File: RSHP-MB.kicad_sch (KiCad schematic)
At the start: 23 parts, among them J1 Conn_02x20_Odd_Even, J2 Conn_02x02_Odd_Even, J3 Conn_02x02_Odd_Even, J4 Conn_02x04_Odd_Even

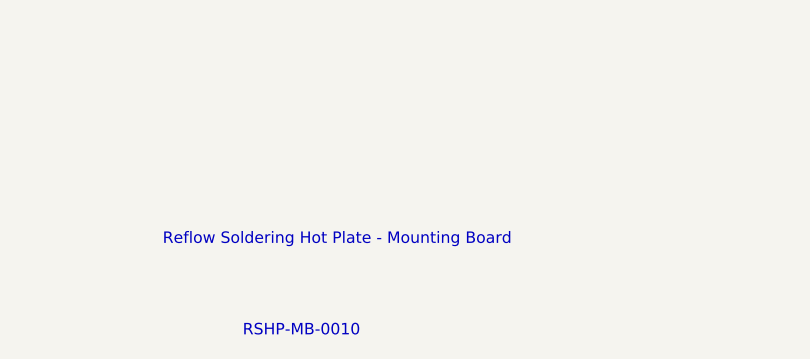
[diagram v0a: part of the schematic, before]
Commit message: Properly filled document metadata
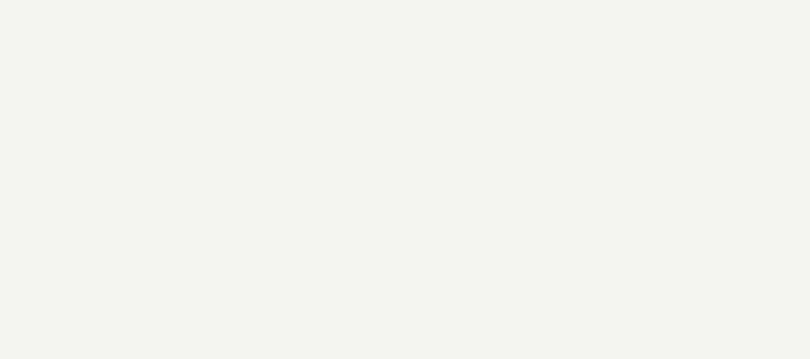
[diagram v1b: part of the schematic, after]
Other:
- note removed: "RSHP-MB-0010"
- note removed: "Reflow Soldering Hot Plate - Mounting Board"
- company: (none) -> (c) Andriy Golovnya http://redscorp.net
- title: (none) -> RSHP-MB-0010
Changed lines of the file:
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@@
 (kicad_sch (version 20211123) (generator eeschema)
   (paper "A4")
+  (title_block
+    (title "RSHP-MB-0010")
+    (date "2022-05-21")
+    (rev "1.0")
+    (company "(c) Andriy Golovnya http://redscorp.net")
+    (comment 1 "Reflow Soldering Hot Plate - Mounting Board")
+  )
   (junction (at 76.2 83.82) (diameter 0) (color 0 0 0 0)
   )
@@
   (wire (pts (xy 39.37 121.92) (xy 39.37 127))
     (stroke (width 0) (type default) (color 0 0 0 0))
-  )
-  (text "RSHP-MB-0010" (at 186.69 190.5 0)
-    (effects (font (size 1.27 1.27)) (justify left bottom))
   )
   (text "Fan Mounting Holes/\nEarth Tranfer Points" (at 134.62 114.3 0)
@@
     (effects (font (size 1.27 1.27) bold) (justify left bottom))
   )
-  (text "Reflow Soldering Hot Plate - Mounting Board" (at 177.8 180.34 0)
-    (effects (font (size 1.27 1.27)) (justify left bottom))
-  )
   (text "Thermal Resistors Connector" (at 198.12 38.1 0)

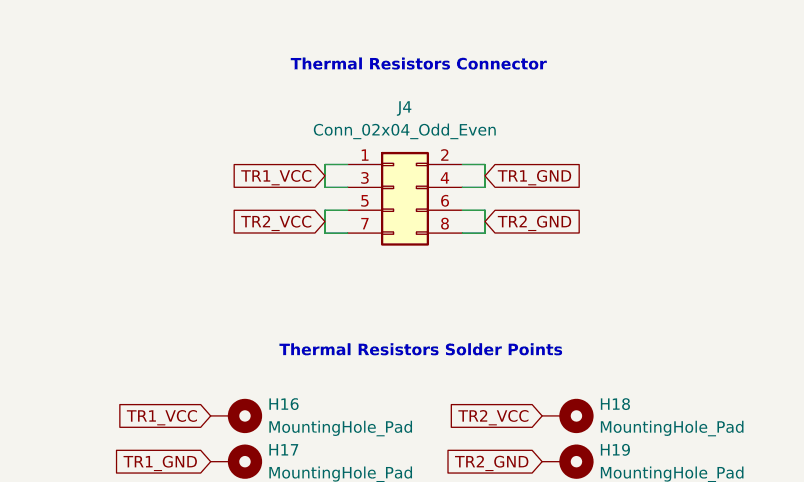
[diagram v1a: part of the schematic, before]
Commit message: Switched TR connector sides in schematics. rounded some corners on PCB.
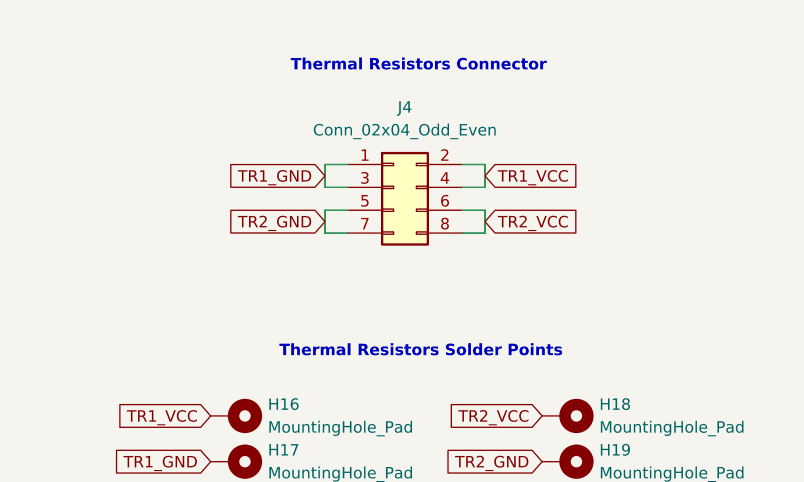
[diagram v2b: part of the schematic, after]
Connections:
- net TR1_GND: now also J4.1 (Pin_1), J4.3 (Pin_3); no longer J4.2 (Pin_2), J4.4 (Pin_4)
- net TR1_VCC: now also J4.2 (Pin_2), J4.4 (Pin_4); no longer J4.1 (Pin_1), J4.3 (Pin_3)
- net TR2_GND: now also J4.5 (Pin_5), J4.7 (Pin_7); no longer J4.6 (Pin_6), J4.8 (Pin_8)
- net TR2_VCC: now also J4.6 (Pin_6), J4.8 (Pin_8); no longer J4.5 (Pin_5), J4.7 (Pin_7)
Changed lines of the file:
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@@
     )
   )
-  (global_label "TR2_VCC" (shape input) (at 201.93 54.61 180) (fields_autoplaced)
-    (effects (font (size 1.27 1.27)) (justify right))
-    (property "Intersheet References" "${INTERSHEET_REFS}" (id 0) (at 191.4736 54.6894 0)
-      (effects (font (size 1.27 1.27)) (justify right) hide)
+  (global_label "TR2_VCC" (shape input) (at 219.71 54.61 0) (fields_autoplaced)
+    (effects (font (size 1.27 1.27)) (justify left))
+    (property "Intersheet References" "${INTERSHEET_REFS}" (id 0) (at 230.1664 54.5306 0)
+      (effects (font (size 1.27 1.27)) (justify left) hide)
     )
   )
-  (global_label "TR2_GND" (shape input) (at 219.71 54.61 0) (fields_autoplaced)
-    (effects (font (size 1.27 1.27)) (justify left))
-    (property "Intersheet References" "${INTERSHEET_REFS}" (id 0) (at 230.4083 54.6894 0)
-      (effects (font (size 1.27 1.27)) (justify left) hide)
+  (global_label "TR2_GND" (shape input) (at 201.93 54.61 180) (fields_autoplaced)
+    (effects (font (size 1.27 1.27)) (justify right))
+    (property "Intersheet References" "${INTERSHEET_REFS}" (id 0) (at 191.2317 54.5306 0)
+      (effects (font (size 1.27 1.27)) (justify right) hide)
     )
   )
@@
     )
   )
-  (global_label "TR1_GND" (shape input) (at 219.71 49.53 0) (fields_autoplaced)
-    (effects (font (size 1.27 1.27)) (justify left))
-    (property "Intersheet References" "${INTERSHEET_REFS}" (id 0) (at 230.4083 49.6094 0)
-      (effects (font (size 1.27 1.27)) (justify left) hide)
+  (global_label "TR1_GND" (shape input) (at 201.93 49.53 180) (fields_autoplaced)
+    (effects (font (size 1.27 1.27)) (justify right))
+    (property "Intersheet References" "${INTERSHEET_REFS}" (id 0) (at 191.2317 49.4506 0)
+      (effects (font (size 1.27 1.27)) (justify right) hide)
     )
   )
@@
     )
   )
-  (global_label "TR1_VCC" (shape input) (at 201.93 49.53 180) (fields_autoplaced)
-    (effects (font (size 1.27 1.27)) (justify right))
-    (property "Intersheet References" "${INTERSHEET_REFS}" (id 0) (at 191.4736 49.6094 0)
-      (effects (font (size 1.27 1.27)) (justify right) hide)
+  (global_label "TR1_VCC" (shape input) (at 219.71 49.53 0) (fields_autoplaced)
+    (effects (font (size 1.27 1.27)) (justify left))
+    (property "Intersheet References" "${INTERSHEET_REFS}" (id 0) (at 230.1664 49.4506 0)
+      (effects (font (size 1.27 1.27)) (justify left) hide)
     )
   )
